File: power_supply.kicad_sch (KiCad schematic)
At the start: 22 parts, among them J1 Conn_01x02, U12 AMS1117-5.0, U3 AP63203WU

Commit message: Use basic parts where possible
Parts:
- C1, C10, C11, C14, C9: footprint Capacitor_SMD:C_0603_1608Metric_Pad1.08x0.95mm_HandSolder -> Capacitor_SMD:C_0603_1608Metric
- C12, C13, C5: footprint Capacitor_SMD:C_0603_1608Metric_Pad1.08x0.95mm_HandSolder -> Capacitor_SMD:C_0603_1608Metric; LCSC PN C2762594 -> C59461
- D1, D2: footprint LED_SMD:LED_0603_1608Metric_Pad1.05x0.95mm_HandSolder -> LED_SMD:LED_0805_2012Metric; LCSC PN C965804 -> C2297
- R1: footprint Resistor_SMD:R_0603_1608Metric_Pad0.98x0.95mm_HandSolder -> Resistor_SMD:R_0603_1608Metric; LCSC PN C112310 -> C23228
- R2: footprint Resistor_SMD:R_0603_1608Metric_Pad0.98x0.95mm_HandSolder -> Resistor_SMD:R_0603_1608Metric; LCSC PN C114433 -> C23179
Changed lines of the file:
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@@
 			)
 		)
-		(property "Footprint" "Capacitor_SMD:C_0603_1608Metric_Pad1.08x0.95mm_HandSolder"
+		(property "Footprint" "Capacitor_SMD:C_0603_1608Metric"
 			(at 115.57 127.9652 0)
 			(effects
@@
 			)
 		)
-		(property "Footprint" "Capacitor_SMD:C_0603_1608Metric_Pad1.08x0.95mm_HandSolder"
+		(property "Footprint" "Capacitor_SMD:C_0603_1608Metric"
 			(at 51.1048 119.38 0)
 			(effects
@@
 			)
 		)
-		(property "Footprint" "Capacitor_SMD:C_0603_1608Metric_Pad1.08x0.95mm_HandSolder"
+		(property "Footprint" "Capacitor_SMD:C_0603_1608Metric"
 			(at 171.1452 119.38 0)
 			(effects
@@
 			)
 		)
-		(property "LCSC PN" "C2762594"
+		(property "LCSC PN" "C59461"
 			(at 170.18 115.57 0)
 			(effects
@@
 			)
 		)
-		(property "Footprint" "Resistor_SMD:R_0603_1608Metric_Pad0.98x0.95mm_HandSolder"
+		(property "Footprint" "Resistor_SMD:R_0603_1608Metric"
 			(at 192.532 111.76 90)
 			(effects
@@
 			)
 		)
-		(property "LCSC PN" "C114433"
+		(property "LCSC PN" "C23179"
 			(at 194.31 111.76 0)
 			(effects
@@
 			)
 		)
-		(property "Footprint" "Capacitor_SMD:C_0603_1608Metric_Pad1.08x0.95mm_HandSolder"
+		(property "Footprint" "Capacitor_SMD:C_0603_1608Metric"
 			(at 123.4948 80.01 0)
 			(effects
@@
 			)
 		)
-		(property "Footprint" "Capacitor_SMD:C_0603_1608Metric_Pad1.08x0.95mm_HandSolder"
+		(property "Footprint" "Capacitor_SMD:C_0603_1608Metric"
 			(at 155.9052 80.01 0)
 			(effects
@@
 			)
 		)
-		(property "LCSC PN" "C2762594"
+		(property "LCSC PN" "C59461"
 			(at 154.94 76.2 0)
 			(effects
@@
 			)
 		)
-		(property "Footprint" "Capacitor_SMD:C_0603_1608Metric_Pad1.08x0.95mm_HandSolder"
+		(property "Footprint" "Capacitor_SMD:C_0603_1608Metric"
 			(at 159.7152 119.38 0)
 			(effects
@@
 			)
 		)
-		(property "LCSC PN" "C2762594"
+		(property "LCSC PN" "C59461"
 			(at 158.75 115.57 0)
 			(effects
@@
 			)
 		)
-		(property "Footprint" "Capacitor_SMD:C_0603_1608Metric_Pad1.08x0.95mm_HandSolder"
+		(property "Footprint" "Capacitor_SMD:C_0603_1608Metric"
 			(at 147.0152 119.38 0)
 			(effects
@@
 			)
 		)
-		(property "Footprint" "LED_SMD:LED_0603_1608Metric_Pad1.05x0.95mm_HandSolder"
+		(property "Footprint" "LED_SMD:LED_0805_2012Metric"
 			(at 194.31 120.65 0)
 			(effects
@@
 			)
 		)
-		(property "Datasheet" "https://www.lcsc.com/datasheet/C965804.pdf"
+		(property "Datasheet" "https://jlcpcb.com/api/file/downloadByFileSystemAccessId/8639582106239348736"
 			(at 194.31 120.65 0)
 			(effects
@@
 			)
 		)
-		(property "LCSC PN" "C965804"
+		(property "LCSC PN" "C2297"
 			(at 194.31 120.65 90)
 			(effects
@@
 			)
 		)
-		(property "Footprint" "LED_SMD:LED_0603_1608Metric_Pad1.05x0.95mm_HandSolder"
+		(property "Footprint" "LED_SMD:LED_0805_2012Metric"
 			(at 179.07 78.74 0)
 			(effects
@@
 			)
 		)
-		(property "Datasheet" "https://www.lcsc.com/datasheet/C965804.pdf"
+		(property "Datasheet" "https://jlcpcb.com/api/file/downloadByFileSystemAccessId/8639582106239348736"
 			(at 179.07 78.74 0)
 			(effects
@@
 			)
 		)
-		(property "LCSC PN" "C965804"
+		(property "LCSC PN" "C2297"
 			(at 179.07 78.74 90)
 			(effects
@@
 			)
 		)
-		(property "Footprint" "Capacitor_SMD:C_0603_1608Metric_Pad1.08x0.95mm_HandSolder"
+		(property "Footprint" "Capacitor_SMD:C_0603_1608Metric"
 			(at 65.0748 119.38 0)
 			(effects
@@
 			)
 		)
-		(property "Footprint" "Resistor_SMD:R_0603_1608Metric_Pad0.98x0.95mm_HandSolder"
+		(property "Footprint" "Resistor_SMD:R_0603_1608Metric"
 			(at 177.292 69.85 90)
 			(effects
@@
 			)
 		)
-		(property "LCSC PN" "C112310"
+		(property "LCSC PN" "C23228"
 			(at 179.07 69.85 0)
 			(effects

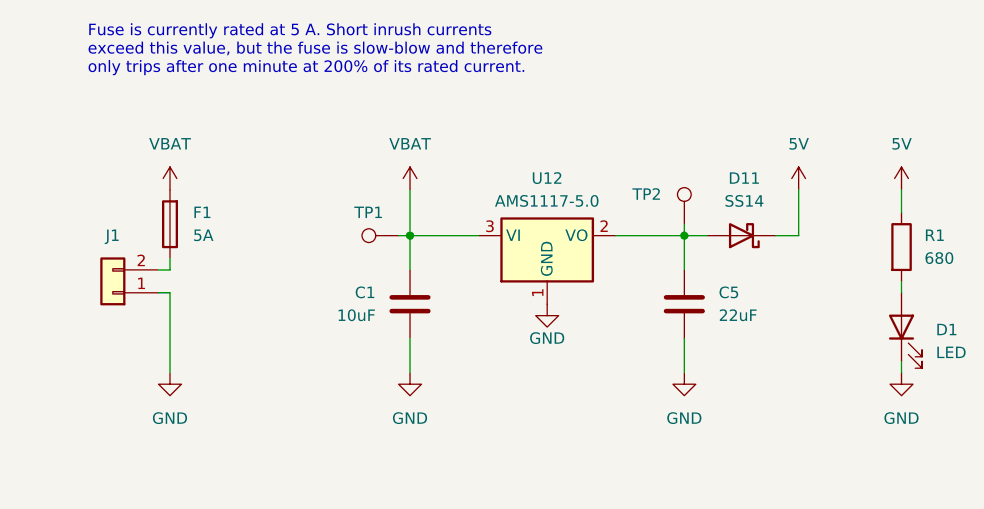
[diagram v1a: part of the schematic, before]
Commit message: Fix bus merging and add net classes
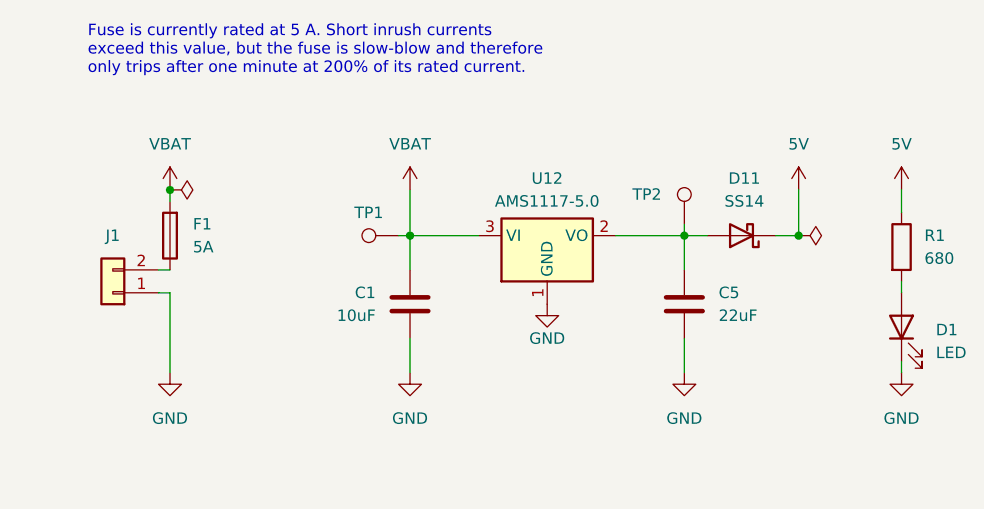
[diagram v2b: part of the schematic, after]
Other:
- moved on the sheet: F1
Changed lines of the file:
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@@
 	)
 	(junction
+		(at 97.79 63.5)
+		(diameter 0)
+		(color 0 0 0 0)
+	)
+	(junction
 		(at 124.46 124.46)
 		(diameter 0)
@@
 	)
 	(junction
+		(at 167.64 68.58)
+		(diameter 0)
+		(color 0 0 0 0)
+	)
+	(junction
 		(at 127 114.3)
 		(diameter 0)
@@
 	(wire
 		(pts
-			(xy 97.79 71.12) (xy 97.79 72.39)
-		)
-		(stroke
-			(width 0)
-			(type default)
-		)
-	)
-	(wire
-		(pts
 			(xy 114.3 119.38) (xy 114.3 127)
 		)
@@
 	(wire
 		(pts
+			(xy 97.79 64.77) (xy 97.79 63.5)
+		)
+		(stroke
+			(width 0)
+			(type default)
+		)
+	)
+	(wire
+		(pts
 			(xy 83.82 113.03) (xy 83.82 114.3)
 		)
@@
 	(symbol
 		(lib_id "Device:Fuse")
-		(at 97.79 67.31 180)
+		(at 97.79 68.58 180)
 		(unit 1)
 		(exclude_from_sim no)
@@
 		(fields_autoplaced yes)
 		(property "Reference" "F1"
-			(at 100.33 66.0399 0)
+			(at 100.33 67.3099 0)
 			(effects
 				(font
@@
 		)
 		(property "Value" "5A"
-			(at 100.33 68.5799 0)
+			(at 100.33 69.8499 0)
 			(effects
 				(font
@@
 		)
 		(property "Footprint" "Fuse:Fuse_Littelfuse-NANO2-451_453"
-			(at 99.568 67.31 90)
+			(at 99.568 68.58 90)
 			(effects
 				(font
@@
 		)
 		(property "Datasheet" "https://www.littelfuse.com/assetdocs/fuse-452-and-454-datasheet?assetguid=8c87aa93-80a7-4ea8-8749-a19ba03901c2"
-			(at 97.79 67.31 0)
+			(at 97.79 68.58 0)
 			(effects
 				(font
@@
 		)
 		(property "Description" "5A 125V Fuse Surface Mount 2410"
-			(at 97.79 67.31 0)
+			(at 97.79 68.58 0)
 			(effects
 				(font
@@
 		)
 		(property "LCSC PN" "C66503"
-			(at 97.79 67.31 0)
+			(at 97.79 68.58 0)
 			(effects
 				(font
@@
 	)
 	(symbol
+		(lib_id "power:PWR_FLAG")
+		(at 97.79 63.5 270)
+		(unit 1)
+		(exclude_from_sim no)
+		(in_bom yes)
+		(on_board yes)
+		(dnp no)
+		(fields_autoplaced yes)
+		(property "Reference" "#FLG02"
+			(at 99.695 63.5 0)
+			(effects
+				(font
+					(size 1.27 1.27)
+				)
+				(hide yes)
+			)
+		)
+		(property "Value" "PWR_FLAG"
+			(at 101.6 63.4999 90)
+			(effects
+				(font
+					(size 1.27 1.27)
+				)
+				(justify left)
+				(hide yes)
+			)
+		)
+		(property "Footprint" ""
+			(at 97.79 63.5 0)
+			(effects
+				(font
+					(size 1.27 1.27)
+				)
+				(hide yes)
+			)
+		)
+		(property "Datasheet" "~"
+			(at 97.79 63.5 0)
+			(effects
+				(font
+					(size 1.27 1.27)
+				)
+				(hide yes)
+			)
+		)
+		(property "Description" "Special symbol for telling ERC where power comes from"
+			(at 97.79 63.5 0)
+			(effects
+				(font
+					(size 1.27 1.27)
+				)
+				(hide yes)
+			)
+		)
+		(pin "1"
+		)
+		(instances
+			(project "Tumbler2_Redesign"
+				(path "/f3fd8d79-9d35-4c04-811e-2697a2740958/003ca151-4f76-4d52-861b-70be86047379"
+					(reference "#FLG02")
+					(unit 1)
+				)
+			)
+		)
+	)
+	(symbol
 		(lib_id "power:GND")
 		(at 158.75 127 0)
@@
 					(unit 1)
 				)
+			)
+		)
+	)
+	(symbol
+		(lib_id "power:PWR_FLAG")
+		(at 167.64 68.58 270)
+		(unit 1)
+		(exclude_from_sim no)
+		(in_bom yes)
+		(on_board yes)
+		(dnp no)
+		(fields_autoplaced yes)
+		(property "Reference" "#FLG01"
+			(at 169.545 68.58 0)
+			(effects
+				(font
+					(size 1.27 1.27)
+				)
+				(hide yes)
+			)
+		)
+		(property "Value" "PWR_FLAG"
+			(at 171.45 68.5799 90)
+			(effects
+				(font
+					(size 1.27 1.27)
+				)
+				(justify left)
+				(hide yes)
+			)
+		)
+		(property "Footprint" ""
+			(at 167.64 68.58 0)
+			(effects
+				(font
+					(size 1.27 1.27)
+				)
+				(hide yes)
+			)
+		)
+		(property "Datasheet" "~"
+			(at 167.64 68.58 0)
+			(effects
+				(font
+					(size 1.27 1.27)
+				)
+				(hide yes)
+			)
+		)
+		(property "Description" "Special symbol for telling ERC where power comes from"
+			(at 167.64 68.58 0)
+			(effects
+				(font
+					(size 1.27 1.27)
+				)
+				(hide yes)
+			)
+		)
+		(pin "1"
+		)
+		(instances
+			(project ""
+				(path "/f3fd8d79-9d35-4c04-811e-2697a2740958/003ca151-4f76-4d52-861b-70be86047379"
+					(reference "#FLG01")
+					(unit 1)
+				)

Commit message: Start conceptual layouting
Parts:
- TP1, TP2, TP4: footprint TestPoint:TestPoint_Pad_D1.5mm -> TestPoint:TestPoint_THTPad_D1.0mm_Drill0.5mm
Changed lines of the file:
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@@
 			)
 		)
-		(property "Footprint" "TestPoint:TestPoint_Pad_D1.5mm"
+		(property "Footprint" "TestPoint:TestPoint_THTPad_D1.0mm_Drill0.5mm"
 			(at 123.19 63.5 0)
 			(effects
@@
 			)
 		)
-		(property "Footprint" "TestPoint:TestPoint_Pad_D1.5mm"
+		(property "Footprint" "TestPoint:TestPoint_THTPad_D1.0mm_Drill0.5mm"
 			(at 149.86 67.31 0)
 			(effects
@@
 			)
 		)
-		(property "Footprint" "TestPoint:TestPoint_Pad_D1.5mm"
+		(property "Footprint" "TestPoint:TestPoint_THTPad_D1.0mm_Drill0.5mm"
 			(at 128.27 119.38 0)
 			(effects

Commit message: Continue layout and update schematic
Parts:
- renumbered C5 to C2, C9 to C3, C10 to C4, C11 to C5, C12 to C6, C13 to C7, C14 to C8, D11 to D1, D1 to D2, D12 to D3, D2 to D4, L2 to L1, TP2 to TP1, TP1 to TP2, TP4 to TP3, U12 to U1, U3 to U2

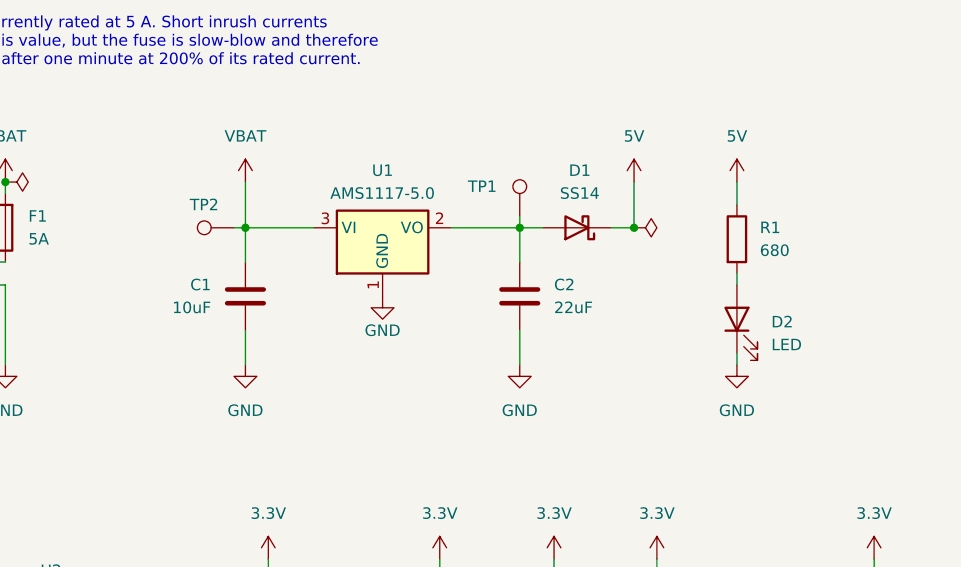
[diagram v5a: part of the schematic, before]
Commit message: cleanup schemati, replaced some caps from 0603 to 0805 around Linear Regulator
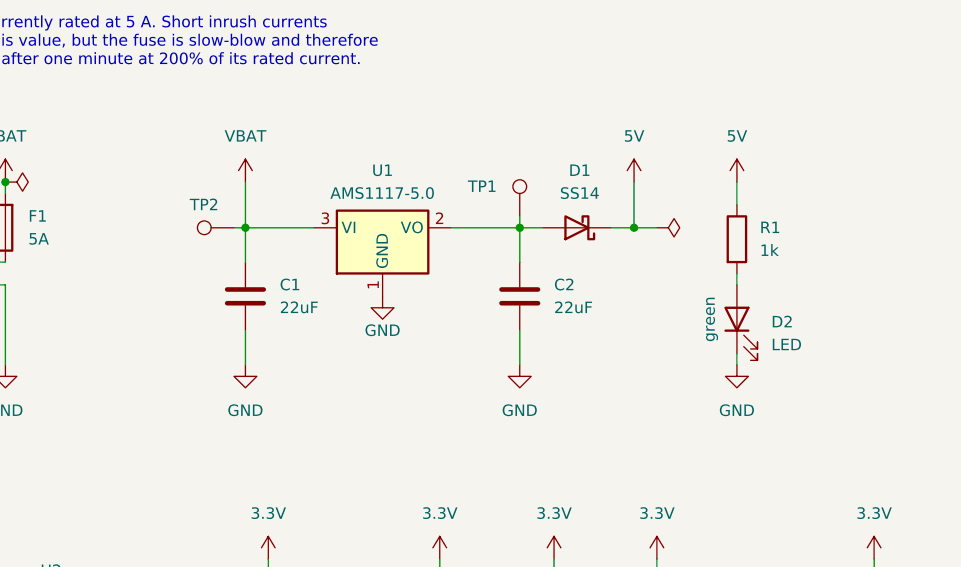
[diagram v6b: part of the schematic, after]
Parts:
- C1: value 10uF -> 22uF; footprint Capacitor_SMD:C_0603_1608Metric -> Capacitor_SMD:C_0805_2012Metric; LCSC PN C96446 -> C45783
- C2, C6, C7: footprint Capacitor_SMD:C_0603_1608Metric -> Capacitor_SMD:C_0805_2012Metric; LCSC PN C59461 -> C45783
- R1: value 680 -> 1k; LCSC PN C23228 -> C21190
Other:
- company: (none) -> ${COMPANY}
- title: Tumbler 2 Redesign -> ${TITLE}
